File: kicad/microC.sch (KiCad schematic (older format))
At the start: 12 parts, among them IC1 ATMEGA1284P-P, SW1 button-touch-6x6mm, X1 16M, X2 32.768Hz

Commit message: initial commit from old repo/branch copy
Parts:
- removed C7, C8: 12p, Capacitors_ThroughHole:C_Rect_L4_W2.5_P2.5, symbol C
- removed X2: 32.768Hz, Crystals:Crystal_Round_Horizontal_3mm_BigPad, symbol Crystal
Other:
- note added: "FREE"
- note removed: "RTC crystal"
- note removed: "Vérifier si on peut trouver un quartz avec condensateur 6pF dans ce cas pas besoin de C externe"
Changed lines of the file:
@@
 Sheet 2 4
 Title "Windlogger digital"
-Date "2017-03-28"
-Rev "1.1.1"
+Date "2017-07-10"
+Rev "1.2.0"
 Comp "ALEEA"
 Comment1 "LONGUET Gilles"
@@
 Main crystal
 $Comp
-L Crystal X2
-U 1 1 5875302A
-P 7225 4675
-F 0 "X2" V 7425 4625 60  0000 C CNN
-F 1 "32.768Hz" V 7000 4650 60  0000 C CNN
-F 2 "Crystals:Crystal_Round_Horizontal_3mm_BigPad" H 7225 4675 60  0001 C CNN
-F 3 "" H 7225 4675 60  0000 C CNN
-	1    7225 4675
-	0    1    -1   0
-$EndComp
-$Comp
-L C C7
-U 1 1 58753031
-P 7550 4525
-F 0 "C7" H 7550 4625 40  0000 L CNN
-F 1 "12p" H 7556 4440 40  0000 L CNN
-F 2 "Capacitors_ThroughHole:C_Rect_L4_W2.5_P2.5" H 7588 4375 30  0001 C CNN
-F 3 "" H 7550 4525 60  0000 C CNN
-	1    7550 4525
-	0    1    1    0
-$EndComp
-$Comp
-L C C8
-U 1 1 58753038
-P 7550 4825
-F 0 "C8" H 7550 4925 40  0000 L CNN
-F 1 "12p" H 7556 4740 40  0000 L CNN
-F 2 "Capacitors_ThroughHole:C_Rect_L4_W2.5_P2.5" H 7588 4675 30  0001 C CNN
-F 3 "" H 7550 4825 60  0000 C CNN
-	1    7550 4825
-	0    1    1    0
-$EndComp
-$Comp
-L GND #PWR08
-U 1 1 5875303F
-P 7825 4675
-F 0 "#PWR08" H 7825 4425 50  0001 C CNN
-F 1 "GND" H 7825 4525 50  0000 C CNN
-F 2 "" H 7825 4675 50  0000 C CNN
-F 3 "" H 7825 4675 50  0000 C CNN
-	1    7825 4675
-	1    0    0    -1
-$EndComp
-$Comp
 L GND #PWR09
 U 1 1 58753045
@@
 $EndComp
 Wire Wire Line
-	6975 4575 6975 4525
-Wire Wire Line
-	6975 4525 7400 4525
-Wire Wire Line
-	6975 4825 7400 4825
-Wire Wire Line
-	6975 4675 6975 4825
-Connection ~ 7225 4525
-Connection ~ 7225 4825
-Wire Wire Line
-	7725 4825 7700 4825
-Wire Wire Line
-	7725 4525 7725 4825
-Wire Wire Line
-	7725 4525 7700 4525
-Wire Wire Line
-	7825 4675 7725 4675
-Connection ~ 7725 4675
-Wire Wire Line
 	2875 2650 2875 2600
-Text Notes 7200 4350 0    60   ~ 0
-RTC crystal
 Text Notes 2600 3250 0    60   ~ 0
 Reset button
@@
 	2700 5625 2400 5625
 Connection ~ 2400 5625
-Text Notes 7950 4550 0    60   ~ 0
-Vérifier si on peut trouver un quartz avec condensateur 6pF dans ce cas pas besoin de C externe
 Text Notes 2350 1150 0    60   ~ 0
 ajouter une pile avec une comparateur pour isoler le micro lorsqu'aucune source d'alimentation n'est disponible pour que le rtc continue à tourner
+Text Notes 7175 4650 0    60   ~ 0
+FREE
 $EndSCHEMATC

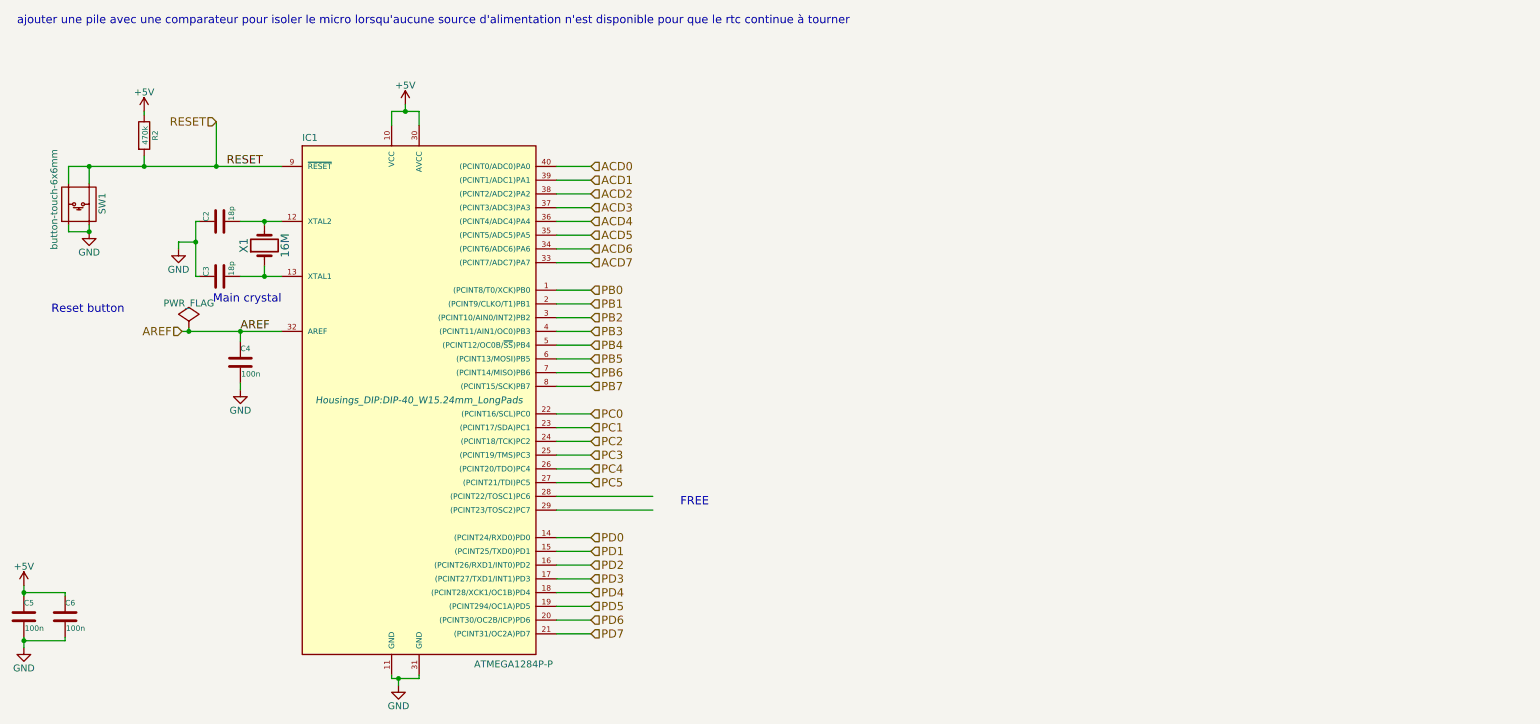
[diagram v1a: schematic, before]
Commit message: Modify micro pins and unify ground in power supply
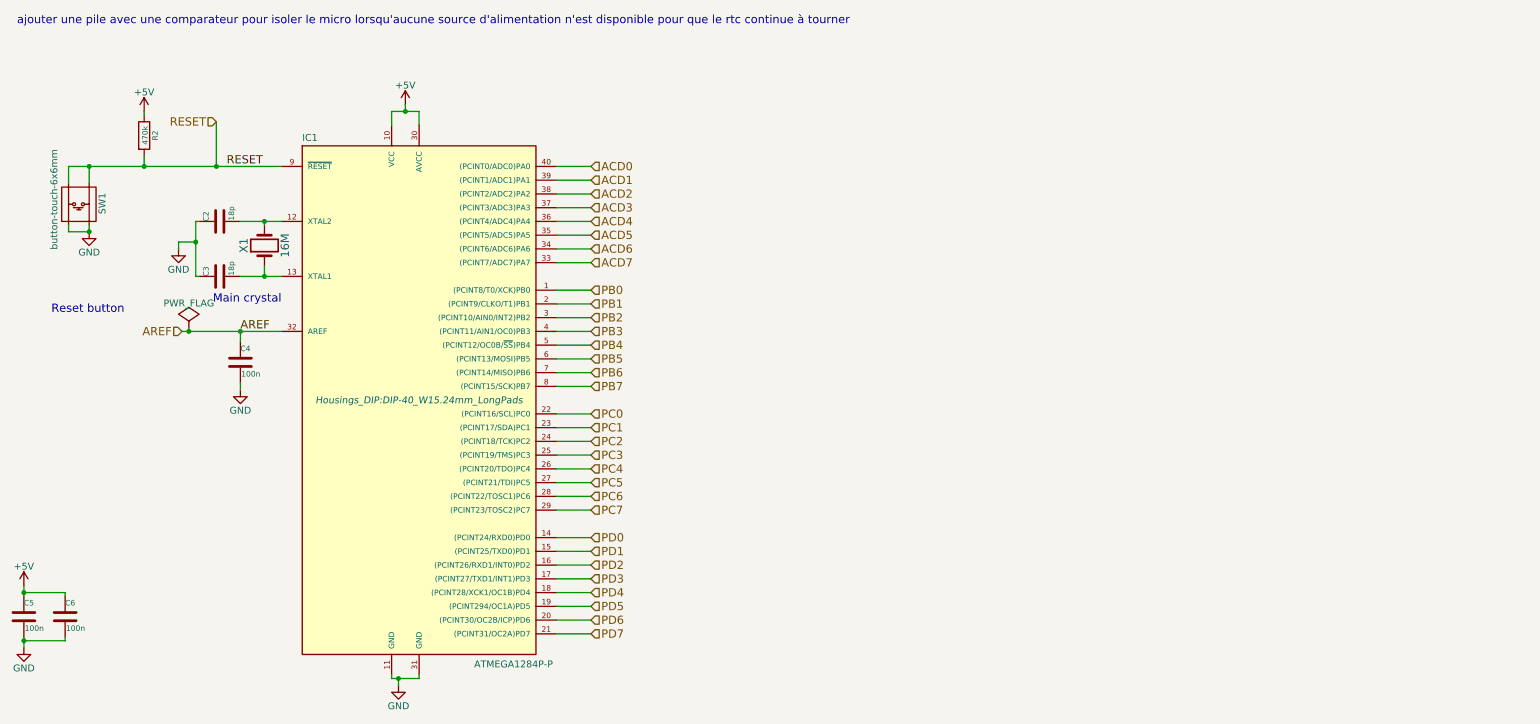
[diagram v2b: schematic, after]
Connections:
- net PC6: now reaches IC1.28 ((PCINT22/TOSC1)PC6)
- net PC7: now reaches IC1.29 ((PCINT23/TOSC2)PC7)
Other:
- note removed: "FREE"
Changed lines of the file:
@@
 	5075 5875 5075 5900
 Wire Wire Line
-	6275 4575 6975 4575
-Wire Wire Line
-	6275 4675 6975 4675
+	6275 4575 6525 4575
+Wire Wire Line
+	6275 4675 6525 4675
 Wire Wire Line
 	5125 5900 5125 5950
@@
 	2875 2175 2875 2300
 Wire Wire Line
-	2725 2175 4275 2175
+	2725 2175 2875 2175
+Wire Wire Line
+	2875 2175 3275 2175
+Wire Wire Line
+	3275 2175 3800 2175
+Wire Wire Line
+	3800 2175 4275 2175
 Wire Wire Line
 	3975 3375 3975 3450
@@
 	3275 1775 3275 1800
 Wire Wire Line
-	3975 2975 4275 2975
+	3975 2975 4150 2975
+Wire Wire Line
+	4150 2975 4275 2975
 Wire Wire Line
 	4150 2900 4150 2975
 Connection ~ 4150 2975
 Wire Wire Line
-	3975 2575 4275 2575
+	3975 2575 4150 2575
+Wire Wire Line
+	4150 2575 4275 2575
 Wire Wire Line
 	4150 2600 4150 2575
@@
 	3650 2975 3675 2975
 Wire Wire Line
-	3650 2575 3650 2975
+	3650 2575 3650 2725
+Wire Wire Line
+	3650 2725 3650 2975
 Wire Wire Line
 	3650 2575 3675 2575
@@
 Connection ~ 3650 2725
 Wire Wire Line
-	2400 5675 2400 5600
-Wire Wire Line
-	2400 5225 2400 5300
+	2400 5675 2400 5625
+Wire Wire Line
+	2400 5625 2400 5600
+Wire Wire Line
+	2400 5225 2400 5275
+Wire Wire Line
+	2400 5275 2400 5300
 $Comp
 L +5V #PWR016
@@
 Connection ~ 3975 3375
 Wire Wire Line
-	3550 3375 4275 3375
+	3550 3375 3600 3375
+Wire Wire Line
+	3600 3375 3975 3375
+Wire Wire Line
+	3975 3375 4275 3375
 Wire Wire Line
 	5075 1875 5075 1775
@@
 Connection ~ 5175 1775
 Wire Wire Line
-	5075 5900 5275 5900
+	5075 5900 5125 5900
+Wire Wire Line
+	5125 5900 5275 5900
 Connection ~ 5125 5900
 $Comp
@@
 $EndComp
 Wire Wire Line
-	5075 1775 5275 1775
+	5075 1775 5175 1775
+Wire Wire Line
+	5175 1775 5275 1775
 Wire Wire Line
 	2700 5300 2700 5275
@@
 Text Notes 2350 1150 0    60   ~ 0
 ajouter une pile avec une comparateur pour isoler le micro lorsqu'aucune source d'alimentation n'est disponible pour que le rtc continue à tourner
-Text Notes 7175 4650 0    60   ~ 0
-FREE
+Text HLabel 6525 4575 2    60   Input ~ 0
+PC6
+Text HLabel 6525 4675 2    60   Input ~ 0
+PC7
 $EndSCHEMATC
